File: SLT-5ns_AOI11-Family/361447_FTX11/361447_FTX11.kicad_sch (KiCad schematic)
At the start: 5 parts, among them T1 IBM_Transistor, T2 IBM_Transistor, T3 IBM_Transistor, T4 IBM_Transistor, U1 12-Pin_SLx_Can

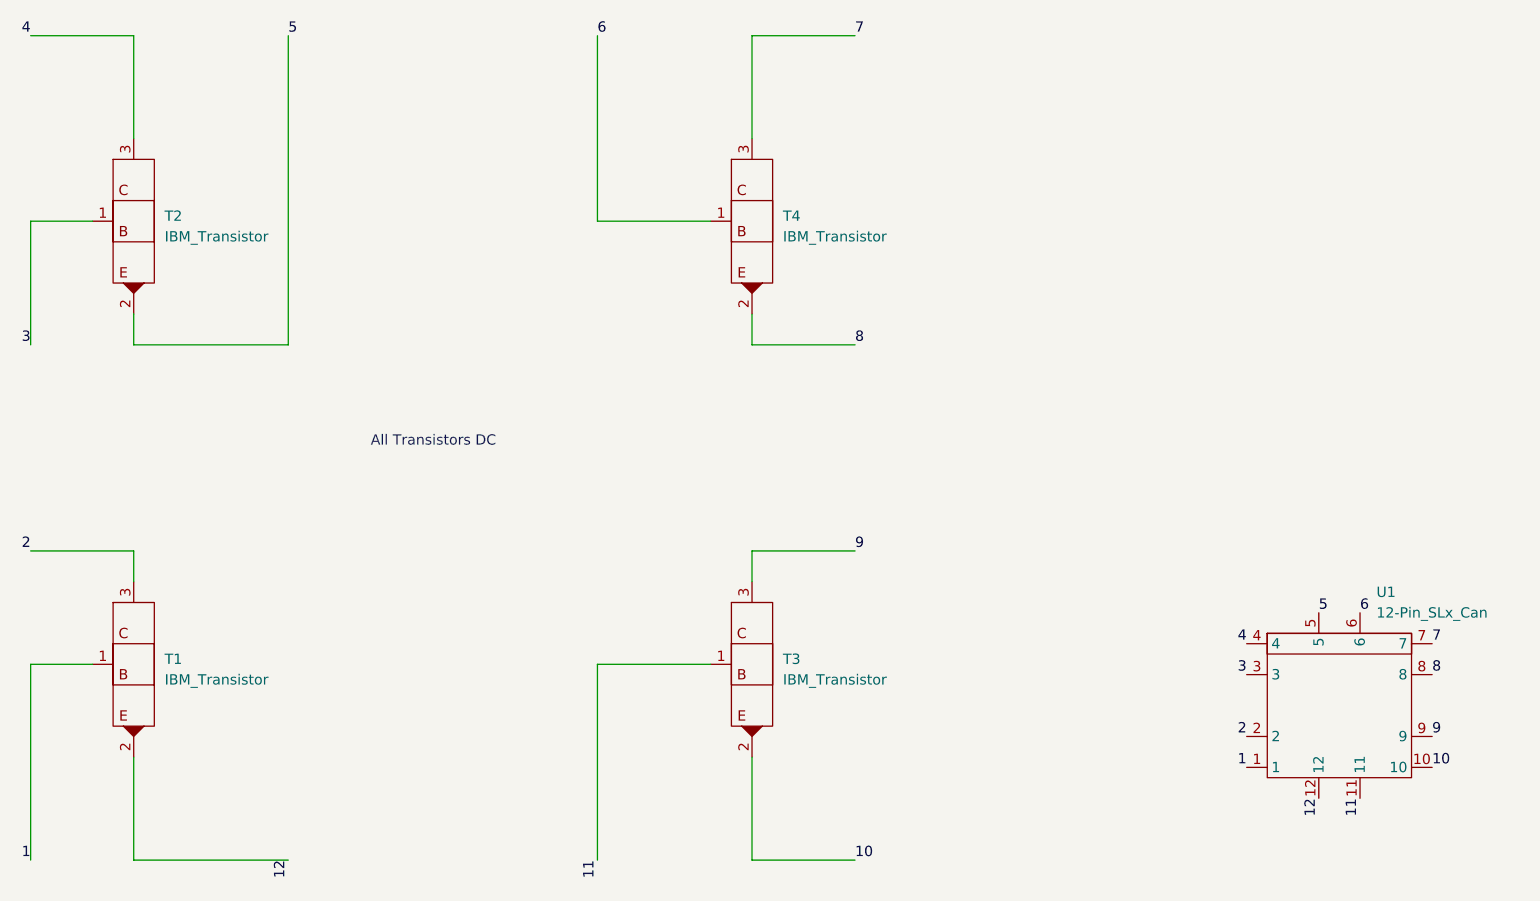
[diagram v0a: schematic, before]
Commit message: Finished off the SLT-30 family of parts, started on the SLT-700 family. Changed labeling of transistors and diodes in all schematics, but have yet to update all the pdf files. This is a TODO...
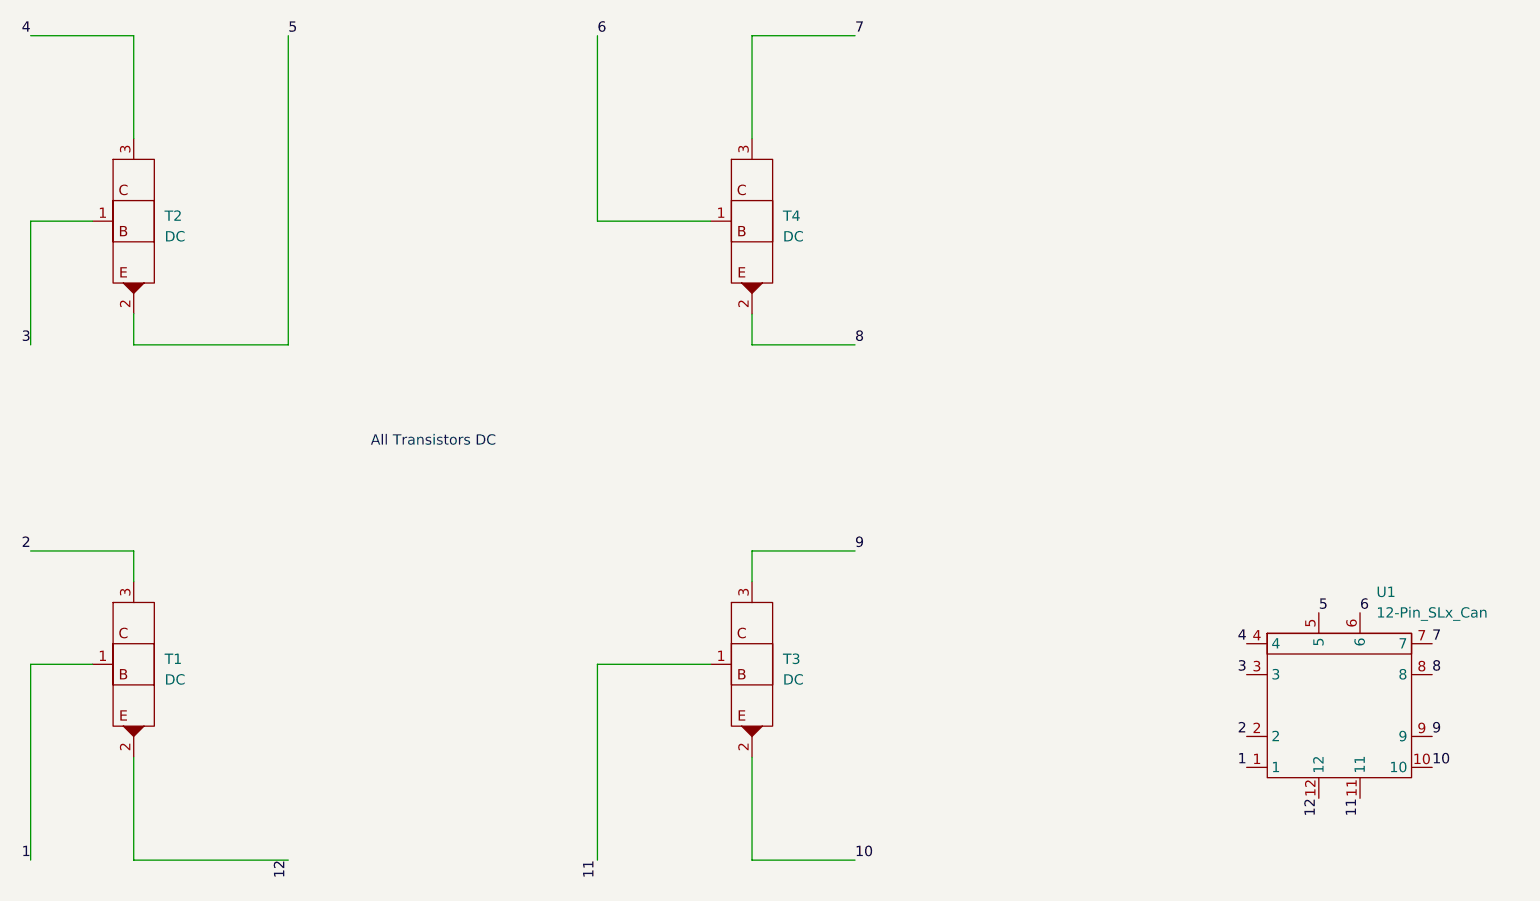
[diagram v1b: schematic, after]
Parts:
- T1, T2, T3, T4: value IBM_Transistor -> DC
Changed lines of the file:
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@@
       (effects (font (size 1.27 1.27)) (justify left))
     )
-    (property "Value" "IBM_Transistor" (id 1) (at 92.71 130.1749 0)
+    (property "Value" "DC" (id 1) (at 92.71 130.1749 0)
       (effects (font (size 1.27 1.27)) (justify left))
     )
@@
       (effects (font (size 1.27 1.27)) (justify left))
     )
-    (property "Value" "IBM_Transistor" (id 1) (at 168.91 75.5649 0)
+    (property "Value" "DC" (id 1) (at 168.91 75.5649 0)
       (effects (font (size 1.27 1.27)) (justify left))
     )
@@
       (effects (font (size 1.27 1.27)) (justify left))
     )
-    (property "Value" "IBM_Transistor" (id 1) (at 92.71 75.5649 0)
+    (property "Value" "DC" (id 1) (at 92.71 75.5649 0)
       (effects (font (size 1.27 1.27)) (justify left))
     )
@@
       (effects (font (size 1.27 1.27)) (justify left))
     )
-    (property "Value" "IBM_Transistor" (id 1) (at 168.91 130.1749 0)
+    (property "Value" "DC" (id 1) (at 168.91 130.1749 0)
       (effects (font (size 1.27 1.27)) (justify left))
     )
@@
   (symbol_instances
     (path "/1f8e8439-29d6-48dc-85a2-31fc4a1324d9"
-      (reference "T1") (unit 1) (value "IBM_Transistor") (footprint "")
+      (reference "T1") (unit 1) (value "DC") (footprint "")
     )
     (path "/89093827-bb23-4e39-8ebb-d4aae8eed604"
-      (reference "T2") (unit 1) (value "IBM_Transistor") (footprint "")
+      (reference "T2") (unit 1) (value "DC") (footprint "")
     )
     (path "/fc223558-0a2b-4b0e-b949-b7fb185c9d35"
-      (reference "T3") (unit 1) (value "IBM_Transistor") (footprint "")
+      (reference "T3") (unit 1) (value "DC") (footprint "")
     )
     (path "/80f5072b-6b7f-47f8-a9c1-14d05fac811f"
-      (reference "T4") (unit 1) (value "IBM_Transistor") (footprint "")
+      (reference "T4") (unit 1) (value "DC") (footprint "")
     )
     (path "/75e072b9-86c1-407b-a1c4-16b7a7044004"
